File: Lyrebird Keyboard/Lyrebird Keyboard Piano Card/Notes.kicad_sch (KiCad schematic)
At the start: 78 parts, among them IC15 CD4024BE, IC16 CD4024BE, IC17 CD4024BE, IC18 CD4024BE, IC19 CD4024BE, IC20 CD4024BE

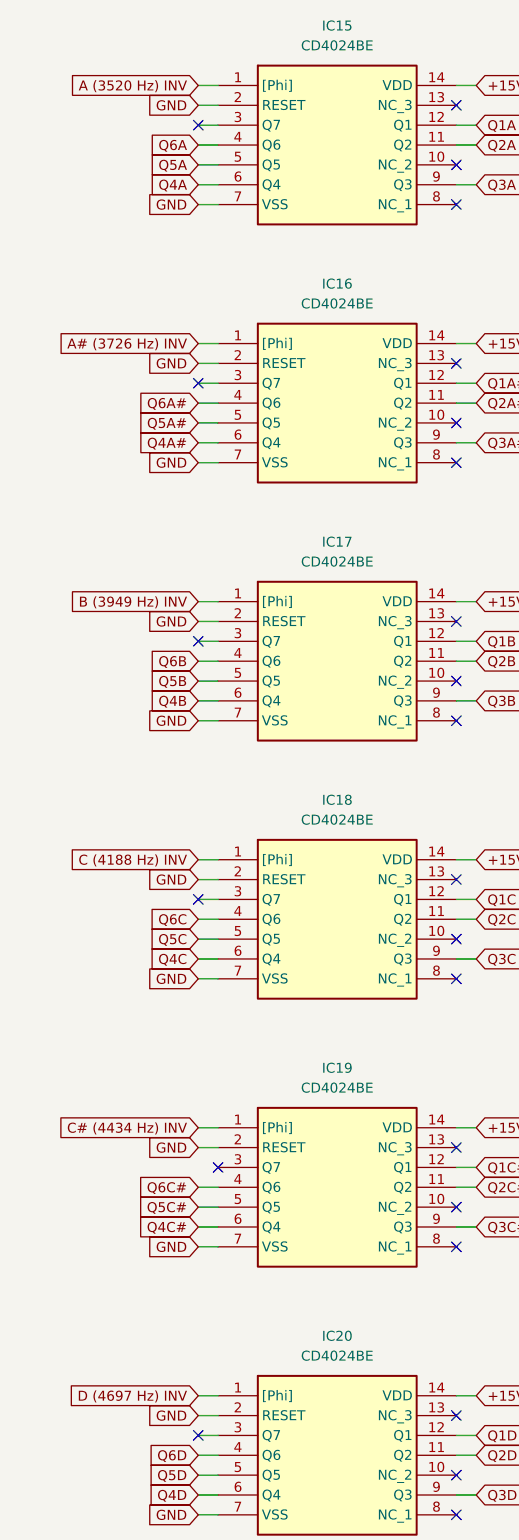
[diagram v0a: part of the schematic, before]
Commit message: Piano Board Layout
Started doing circuit that creates the piano sound.
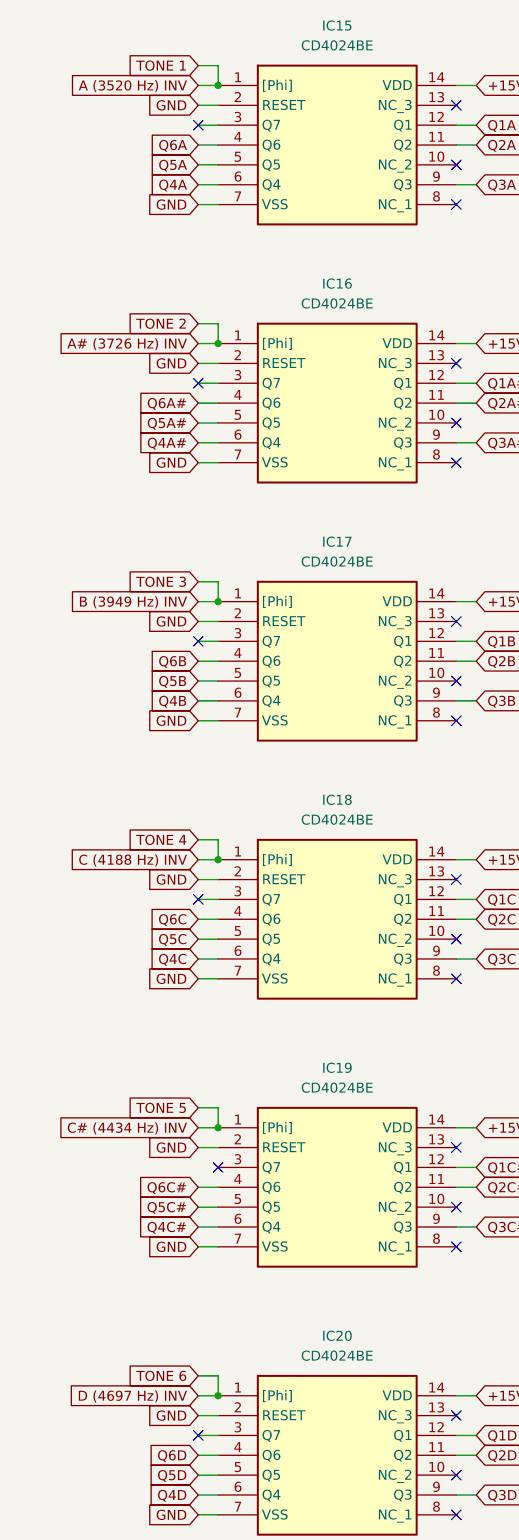
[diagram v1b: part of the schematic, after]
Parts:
- IC15, IC16, IC17, IC18, IC19, IC20: footprint DIP794W53P254L1930H508Q14N -> SamacSys_Parts:DIP794W53P254L1930H508Q14N
